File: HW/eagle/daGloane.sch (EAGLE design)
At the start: 110 parts, among them IC1 MCP1252-33X50, U1 STM32F10XTXU6, X2 SPARKFUN-CONNECTORS_USB-MICROB

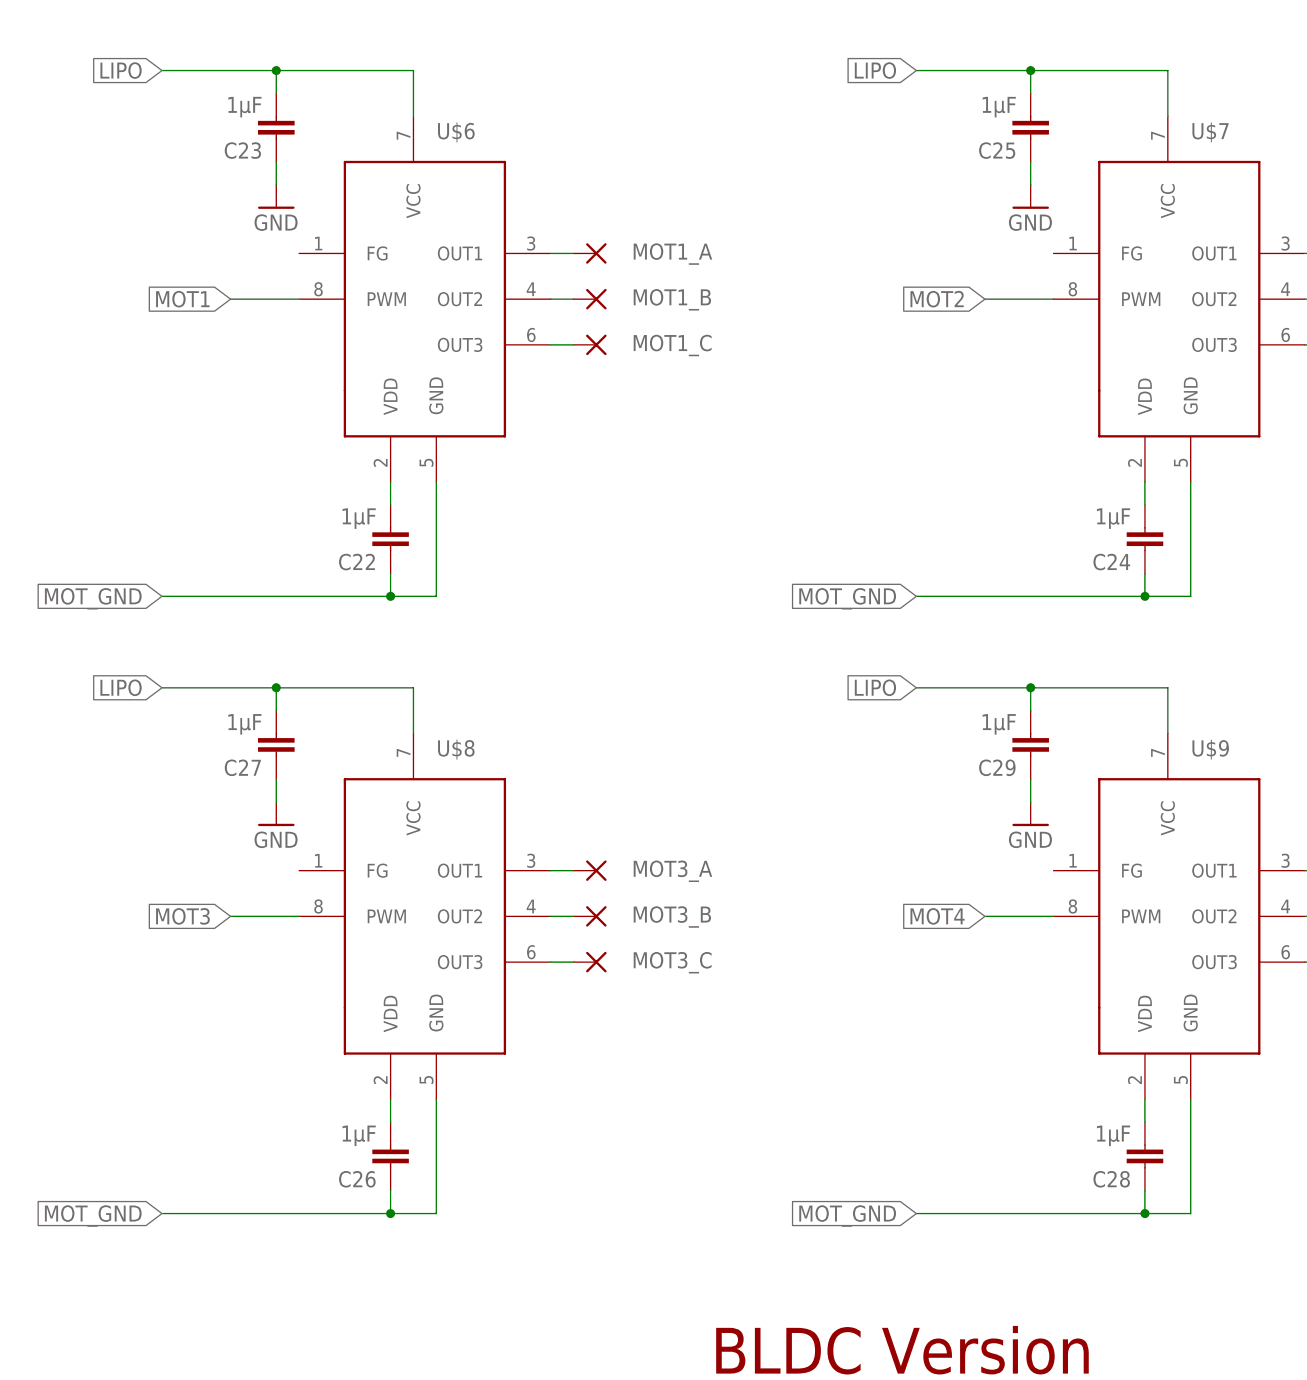
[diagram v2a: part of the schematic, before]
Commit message: gnd connection of decoppling capacitors of BLDC motor drivers changed to mot_gnd
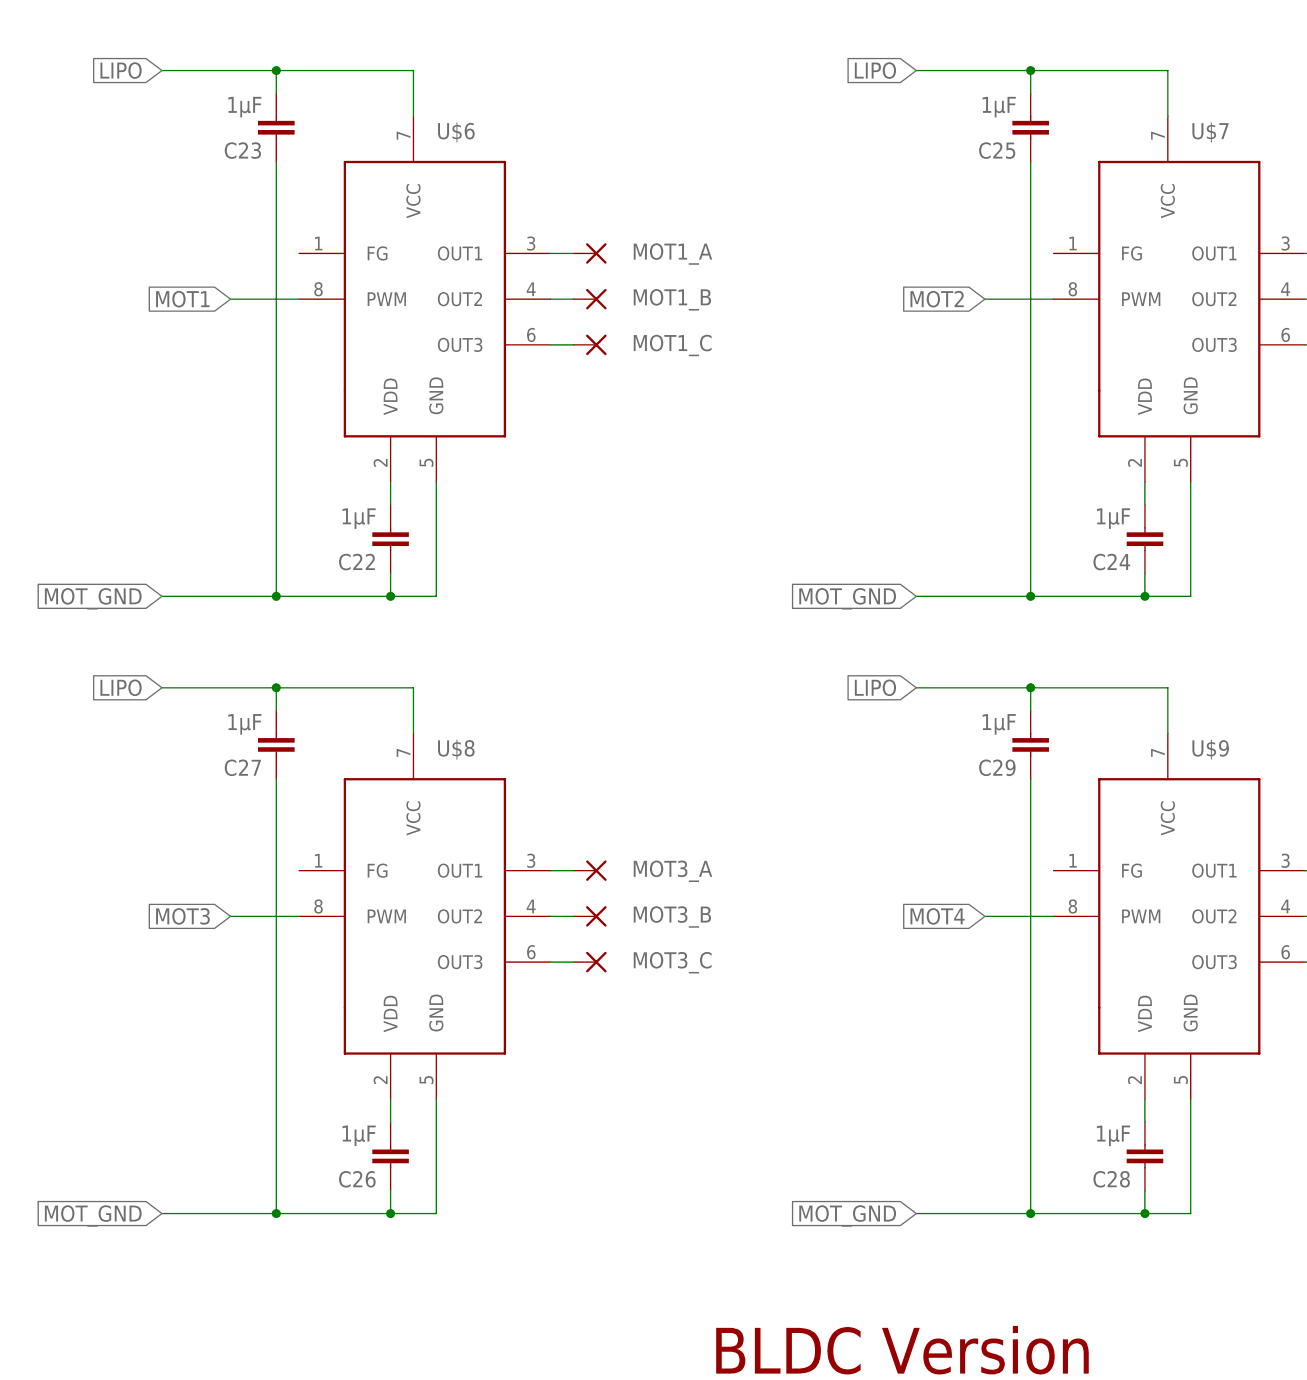
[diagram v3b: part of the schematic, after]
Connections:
- net GND: no longer C23.1, C25.1, C27.1, C29.1
- net MOT_GND: now also C23.1, C25.1, C27.1, C29.1
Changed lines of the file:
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@@
 <?xml version="1.0" encoding="utf-8"?>
 <!DOCTYPE eagle SYSTEM "eagle.dtd">
-<eagle version="6.1">
+<eagle version="6.2">
 <drawing>
 <settings>
@@
 <part name="C22" library="rcl" deviceset="C-EU" device="C0603" value="1µF"/>
 <part name="C23" library="rcl" deviceset="C-EU" device="C0603" value="1µF"/>
-<part name="GND19" library="supply1" deviceset="GND" device=""/>
 <part name="MOT1_A" library="wirepad" deviceset="WIREPAD" device="1,6/0,8"/>
 <part name="MOT1_B" library="wirepad" deviceset="WIREPAD" device="1,6/0,8"/>
@@
 <part name="C24" library="rcl" deviceset="C-EU" device="C0603" value="1µF"/>
 <part name="C25" library="rcl" deviceset="C-EU" device="C0603" value="1µF"/>
-<part name="GND21" library="supply1" deviceset="GND" device=""/>
 <part name="MOT2_A" library="wirepad" deviceset="WIREPAD" device="1,6/0,8"/>
 <part name="MOT2_B" library="wirepad" deviceset="WIREPAD" device="1,6/0,8"/>
@@
 <part name="C26" library="rcl" deviceset="C-EU" device="C0603" value="1µF"/>
 <part name="C27" library="rcl" deviceset="C-EU" device="C0603" value="1µF"/>
-<part name="GND23" library="supply1" deviceset="GND" device=""/>
 <part name="MOT3_A" library="wirepad" deviceset="WIREPAD" device="1,6/0,8"/>
 <part name="MOT3_B" library="wirepad" deviceset="WIREPAD" device="1,6/0,8"/>
@@
 <part name="C28" library="rcl" deviceset="C-EU" device="C0603" value="1µF"/>
 <part name="C29" library="rcl" deviceset="C-EU" device="C0603" value="1µF"/>
-<part name="GND25" library="supply1" deviceset="GND" device=""/>
 <part name="MOT4_A" library="wirepad" deviceset="WIREPAD" device="1,6/0,8"/>
 <part name="MOT4_B" library="wirepad" deviceset="WIREPAD" device="1,6/0,8"/>
@@
 <instance part="C22" gate="G$1" x="414.02" y="-81.28" rot="R180"/>
 <instance part="C23" gate="G$1" x="401.32" y="-35.56" rot="R180"/>
-<instance part="GND19" gate="1" x="401.32" y="-43.18"/>
 <instance part="MOT1_A" gate="G$1" x="436.88" y="-48.26" smashed="yes" rot="R180">
 <attribute name="NAME" x="440.817" y="-48.9458" size="1.778" layer="95"/>
@@
 <instance part="C24" gate="G$1" x="497.84" y="-81.28" rot="R180"/>
 <instance part="C25" gate="G$1" x="485.14" y="-35.56" rot="R180"/>
-<instance part="GND21" gate="1" x="485.14" y="-43.18"/>
 <instance part="MOT2_A" gate="G$1" x="520.7" y="-48.26" smashed="yes" rot="R180">
 <attribute name="NAME" x="524.637" y="-48.9458" size="1.778" layer="95"/>
@@
 <instance part="C26" gate="G$1" x="414.02" y="-149.86" rot="R180"/>
 <instance part="C27" gate="G$1" x="401.32" y="-104.14" rot="R180"/>
-<instance part="GND23" gate="1" x="401.32" y="-111.76"/>
 <instance part="MOT3_A" gate="G$1" x="436.88" y="-116.84" smashed="yes" rot="R180">
 <attribute name="NAME" x="440.817" y="-117.5258" size="1.778" layer="95"/>
@@
 <instance part="C28" gate="G$1" x="497.84" y="-149.86" rot="R180"/>
 <instance part="C29" gate="G$1" x="485.14" y="-104.14" rot="R180"/>
-<instance part="GND25" gate="1" x="485.14" y="-111.76"/>
 <instance part="MOT4_A" gate="G$1" x="520.7" y="-116.84" smashed="yes" rot="R180">
 <attribute name="NAME" x="524.637" y="-117.5258" size="1.778" layer="95"/>
@@
 </segment>
 <segment>
-<pinref part="C23" gate="G$1" pin="1"/>
-<pinref part="GND19" gate="1" pin="GND"/>
-<wire x1="401.32" y1="-40.64" x2="401.32" y2="-38.1" width="0.1524" layer="91"/>
-</segment>
-<segment>
-<pinref part="C25" gate="G$1" pin="1"/>
-<pinref part="GND21" gate="1" pin="GND"/>
-<wire x1="485.14" y1="-40.64" x2="485.14" y2="-38.1" width="0.1524" layer="91"/>
-</segment>
-<segment>
-<pinref part="C27" gate="G$1" pin="1"/>
-<pinref part="GND23" gate="1" pin="GND"/>
-<wire x1="401.32" y1="-109.22" x2="401.32" y2="-106.68" width="0.1524" layer="91"/>
-</segment>
-<segment>
-<pinref part="C29" gate="G$1" pin="1"/>
-<pinref part="GND25" gate="1" pin="GND"/>
-<wire x1="485.14" y1="-109.22" x2="485.14" y2="-106.68" width="0.1524" layer="91"/>
-</segment>
-<segment>
 <pinref part="U$10" gate="G$1" pin="S"/>
 <pinref part="GND18" gate="1" pin="GND"/>
@@
 <wire x1="414.02" y1="-83.82" x2="414.02" y2="-86.36" width="0.1524" layer="91"/>
 <wire x1="414.02" y1="-86.36" x2="419.1" y2="-86.36" width="0.1524" layer="91"/>
-<wire x1="414.02" y1="-86.36" x2="388.62" y2="-86.36" width="0.1524" layer="91"/>
+<wire x1="414.02" y1="-86.36" x2="401.32" y2="-86.36" width="0.1524" layer="91"/>
 <junction x="414.02" y="-86.36"/>
 <label x="388.62" y="-86.36" size="1.778" layer="95" rot="R180" xref="yes"/>
+<pinref part="C23" gate="G$1" pin="1"/>
+<wire x1="401.32" y1="-86.36" x2="388.62" y2="-86.36" width="0.1524" layer="91"/>
+<wire x1="401.32" y1="-38.1" x2="401.32" y2="-86.36" width="0.1524" layer="91"/>
+<junction x="401.32" y="-86.36"/>
 </segment>
 <segment>
-<wire x1="497.84" y1="-86.36" x2="472.44" y2="-86.36" width="0.1524" layer="91"/>
+<wire x1="497.84" y1="-86.36" x2="485.14" y2="-86.36" width="0.1524" layer="91"/>
 <label x="472.44" y="-86.36" size="1.778" layer="95" rot="R180" xref="yes"/>
 <pinref part="U$7" gate="G$1" pin="GND"/>
 <pinref part="C24" gate="G$1" pin="1"/>
+<wire x1="485.14" y1="-86.36" x2="472.44" y2="-86.36" width="0.1524" layer="91"/>
 <wire x1="502.92" y1="-86.36" x2="502.92" y2="-73.66" width="0.1524" layer="91"/>
 <wire x1="497.84" y1="-83.82" x2="497.84" y2="-86.36" width="0.1524" layer="91"/>
 <wire x1="497.84" y1="-86.36" x2="502.92" y2="-86.36" width="0.1524" layer="91"/>
 <junction x="497.84" y="-86.36"/>
+<pinref part="C25" gate="G$1" pin="1"/>
+<wire x1="485.14" y1="-38.1" x2="485.14" y2="-86.36" width="0.1524" layer="91"/>
+<junction x="485.14" y="-86.36"/>
 </segment>
 <segment>
-<wire x1="414.02" y1="-154.94" x2="388.62" y2="-154.94" width="0.1524" layer="91"/>
+<wire x1="414.02" y1="-154.94" x2="401.32" y2="-154.94" width="0.1524" layer="91"/>
 <label x="388.62" y="-154.94" size="1.778" layer="95" rot="R180" xref="yes"/>
 <pinref part="U$8" gate="G$1" pin="GND"/>
 <pinref part="C26" gate="G$1" pin="1"/>
+<wire x1="401.32" y1="-154.94" x2="388.62" y2="-154.94" width="0.1524" layer="91"/>
 <wire x1="419.1" y1="-154.94" x2="419.1" y2="-142.24" width="0.1524" layer="91"/>
 <wire x1="414.02" y1="-152.4" x2="414.02" y2="-154.94" width="0.1524" layer="91"/>
 <wire x1="414.02" y1="-154.94" x2="419.1" y2="-154.94" width="0.1524" layer="91"/>
 <junction x="414.02" y="-154.94"/>
+<pinref part="C27" gate="G$1" pin="1"/>
+<wire x1="401.32" y1="-106.68" x2="401.32" y2="-154.94" width="0.1524" layer="91"/>
+<junction x="401.32" y="-154.94"/>
 </segment>
 <segment>
-<wire x1="497.84" y1="-154.94" x2="472.44" y2="-154.94" width="0.1524" layer="91"/>
+<wire x1="497.84" y1="-154.94" x2="485.14" y2="-154.94" width="0.1524" layer="91"/>
 <label x="472.44" y="-154.94" size="1.778" layer="95" rot="R180" xref="yes"/>
 <pinref part="U$9" gate="G$1" pin="GND"/>
 <pinref part="C28" gate="G$1" pin="1"/>
+<wire x1="485.14" y1="-154.94" x2="472.44" y2="-154.94" width="0.1524" layer="91"/>
 <wire x1="502.92" y1="-154.94" x2="502.92" y2="-142.24" width="0.1524" layer="91"/>
 <wire x1="497.84" y1="-152.4" x2="497.84" y2="-154.94" width="0.1524" layer="91"/>
 <wire x1="497.84" y1="-154.94" x2="502.92" y2="-154.94" width="0.1524" layer="91"/>
 <junction x="497.84" y="-154.94"/>
+<pinref part="C29" gate="G$1" pin="1"/>
+<wire x1="485.14" y1="-106.68" x2="485.14" y2="-154.94" width="0.1524" layer="91"/>
+<junction x="485.14" y="-154.94"/>
 </segment>
 <segment>
